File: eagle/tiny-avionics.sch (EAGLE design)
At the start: 67 parts, among them J1 USB-MICROB, J3 JST-PH-2-SMT-RA, U1 LP5907, U2 M25P10-AVMN6TP_TR, U3 LSM9DS0, U5 LTC1998, U6 ATMEGA32U4-AU, X1 8MHz

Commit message: Reverted board files on master to known-good version
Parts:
- removed U$1: BQ21040, tinyav-lib:BQ21040
- removed U$2: LSM6DS3, tinyav-lib:LSM6DS3
- added IC1: BQ24022, tinyav-lib:BQ24022
- added LED3: (no value), adafruit:LEDCHIP-LED0603
- added R14: 330, rcl:R-US_R0805
- added TP18: TPTP08R, testpad:TPTP08R
- R1: value 5.36k -> 4k; device rcl:R-US_R0805 -> rcl:R-US_R0603
- R15, R16, R6, R7, R8: value 3.3k -> 330
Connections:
- new net N$50: IC1G$1.STAT1, R15.2
- new net N$51: IC1G$1.STAT2, R14.2
- new net N$68: IC1G$1./PG, TP18.TP
- net GND: now also IC1G$1./CE, IC1G$1.ISET2, IC1G$1.VSS; no longer U$1.GND
- net N$13: now also IC1G$1.OUT; no longer U$1.OUT
- net N$4: now also IC1G$1.ISET1, R1.2; no longer R15.2, U$1./CHG
- net N$49: now also LED3.C, R14.1; no longer R1.2, U$1.ISET
- net VBUS1: now also IC1G$1.USB, LED3.A; no longer U$1.VIN
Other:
- moved on the sheet: J1, LED2, R1, R15

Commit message: Merge commit to overwrite eagle files
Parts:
- removed C4: .22µ, rcl:C-EUC0603
- removed C9: 2.2µ, rcl:C-EUC0603
- removed IC1: BQ24022, tinyav-lib:BQ24022
- removed LED3: (no value), adafruit:LEDCHIP-LED0603
- removed R14: 330, rcl:R-US_R0805
- removed R9: 0, rcl:R-US_R0603
- removed TP16, TP17, TP18: TPTP08R, testpad:TPTP08R
- added U$1: 10k B25/50=3375k, tinyav-lib:THERMISTOR-SMD0603
- added U4: BQ21040, tinyav-lib:BQ21040
- C2: device rcl:C-EUC0805 -> rcl:C-EUC0603
- C3: value 4.7µ -> 2.2µ
- R1: value 4k -> 5.36k
- R15, R16, R6, R7, R8: value 330 -> 3.3k; device rcl:R-US_R0805 -> rcl:R-US_R0603
- R2: device rcl:R-US_R0805 -> rcl:R-US_R0603
- U2: value M25P10-AVMN6TP_TR -> M25PX16; device SOIC127P600X175-8N:M25P10-AVMN6TP_TR -> tinyav-lib:M25PX16
- U3: value LSM9DS0 -> LSM6DS3; device LSM9DS0:LSM9DS0 -> tinyav-lib:LSM6DS3
- X1: device IQD-Frequency-Products:CRYSTALS-NOGND-HC49/4H -> tinyav-lib:CRYSTAL-NOGND-SMD
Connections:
- net N$52 renamed TP3
- net N$54 renamed TP12
- net N$55 renamed TP11
- net N$56 renamed TP10
- net N$57 renamed TP9
- net N$58 renamed TP8
- net N$59 renamed TP7
- net N$60 renamed TP1
- net N$61 renamed TP2
- net N$62 renamed TP4
- net N$63 renamed TP5
- net N$64 renamed TP6
- removed net GYR_EN: R9.1, U3.CS(G)
- removed net N$16: U3.INT2(XM), U6.PD2(INT2/RXD1)
- removed net N$17: U3.INT1(XM), U6.PD1(INT1/SDA)
- removed net N$19: U3.INT(G), U6.PD0(INT0/OC0B/SCL)
- removed net N$20: R9.2, U6.PF5(ADC5/TMS)
- removed net N$50: IC1G$1.STAT1, R15.2
- removed net N$51: IC1G$1.STAT2, R14.2
- removed net N$66: TP17.TP, U3.DEN(G)
- removed net N$67: TP16.TP, U3.DRDY(G)
- removed net N$68: IC1G$1./PG, TP18.TP
- net CLK: now also U2.CLK; no longer U2.C
- net GND: now also C3.2, U$1.2, U3.GND2, U3.SCX, U3.SDX, U4.GND; no longer C3.1, C9.2, IC1G$1./CE, IC1G$1.ISET2, IC1G$1.VSS
- net MEM_EN: now also U2./S; no longer U2.~S
- net MISO: now also U2.DQ1(MISO), U3.SDO/SA0; no longer U2.Q, U3.SDO(G), U3.SDO(XM)
- net MOSI: now also U2.DQ0(MOSI); no longer U2.D
- net N$10: now also U3.INT1, U6.PD0(INT0/OC0B/SCL); no longer C4.2, U3.SETC
- net N$11: now also U3.INT2, U6.PD1(INT1/SDA); no longer C4.1, U3.SETP
- net N$13: now also U4.OUT; no longer IC1G$1.OUT
- net N$4: now also R15.2, U4.!CHG; no longer IC1G$1.ISET1, R1.2
- net N$49: now also R1.2, U4.ISET; no longer LED3.C, R14.1
- net N$9: now also U$1.1, U4.TS; no longer C3.2, U3.C1
- net VBUS1: now also U4.VIN; no longer IC1G$1.USB, LED3.A
- net VCC: now also C3.1, U2./HOLD, U2./WP, U3.VDDIO; no longer C9.1, U2.~HOLD, U2.~W, U3.VDD_IO
- net XM_EN: now also U3.CS; no longer U3.CS(XM)
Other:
- note added: "100 mA charge"
- note added: "16Meg Flash Memory"
- note removed: "1Meg Flash Memory"
- note removed: "6-DOF Accelerometer/ Gyroscope"
- moved on the sheet: C15, C16, C17, C18, C3, C5, C6, J1, LED2, R1, R10, R11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

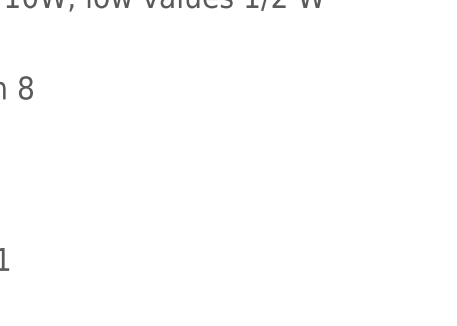
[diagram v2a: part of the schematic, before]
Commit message: Added documentation from google drive. Added board and schematic images.
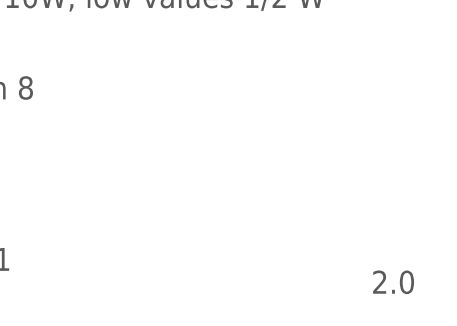
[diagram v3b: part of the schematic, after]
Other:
- note added: "2.0"
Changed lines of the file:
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@@
 <text x="138.938" y="255.778" size="1.778" layer="97">U1</text>
 <text x="54.102" y="212.344" size="1.778" layer="97" rot="R90">100 mA charge</text>
+<text x="416.56" y="7.62" size="2.54" layer="97">2.0</text>
 </plain>
 <instances>
